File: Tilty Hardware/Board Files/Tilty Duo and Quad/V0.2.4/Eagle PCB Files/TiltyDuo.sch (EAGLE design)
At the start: 49 parts, among them U1 TEENSY_3.0_OUTER-PINS28-DIP_S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, U2 HC-09_BREAKOUT, U3 MPL3115A2LGA8, U4 LM2931, U5 MPU-6050, U6 HMC5883LSMD, U7 SPI_FLASH-X25XXSMD

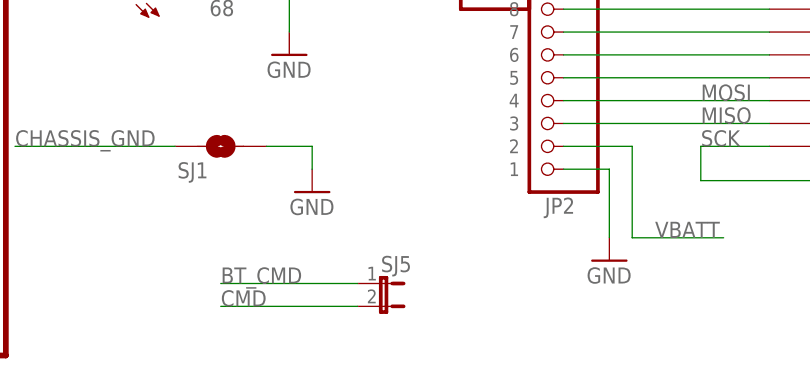
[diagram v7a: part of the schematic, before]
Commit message: Updated bluetooth command jumper to a cuttable trace solder jumper
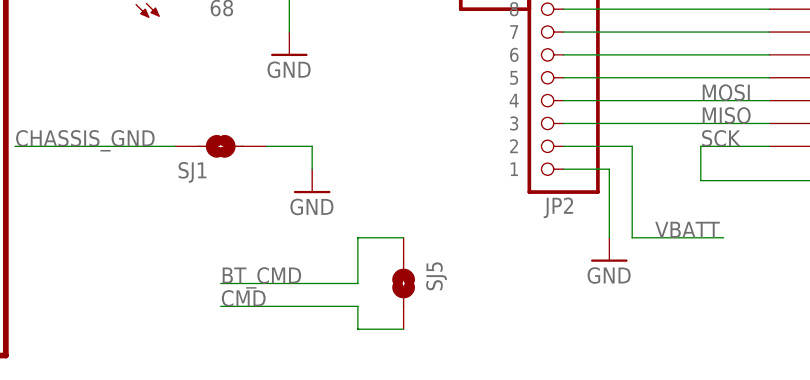
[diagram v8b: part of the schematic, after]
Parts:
- SJ5: value (none) -> SOLDERJUMPERTRACE; device SparkFun-Passives:JUMPER-2SMD-NC -> SparkFun-Passives:SOLDERJUMPERTRACE
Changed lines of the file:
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@@
 <part name="R4" library="resistor" deviceset="R-US_" device="R0603" value="68"/>
 <part name="SJ4" library="SparkFun-Passives" deviceset="SOLDERJUMPER" device="TRACE"/>
-<part name="SJ5" library="SparkFun-Passives" deviceset="JUMPER-2" device="SMD-NC"/>
 <part name="D4" library="SparkFun-DiscreteSemi" deviceset="DIODE" device="SOT23">
 <attribute name="PART#" value="BAT54FSTR-ND"/>
@@
 <part name="SJ6" library="SparkFun-Passives" deviceset="SOLDERJUMPER" device="TRACE"/>
 <part name="D6" library="diode" deviceset="DIODE-" device="DO214AA"/>
+<part name="SJ5" library="SparkFun-Passives" deviceset="SOLDERJUMPER" device="TRACE"/>
 </parts>
 <sheets>
@@
 <attribute name="NAME" x="105.41" y="71.12" size="1.778" layer="95"/>
 </instance>
-<instance part="SJ5" gate="A" x="129.54" y="10.16" rot="R270"/>
 <instance part="D4" gate="G$1" x="218.44" y="60.96" rot="R180">
 <attribute name="PART#" x="218.44" y="60.96" size="1.778" layer="96" rot="R180" display="off"/>
@@
 <attribute name="NAME" x="127" y="121.4374" size="1.778" layer="95" rot="R180"/>
 <attribute name="VALUE" x="124.2314" y="121.92" size="1.778" layer="96" rot="R90"/>
+</instance>
+<instance part="SJ5" gate="1" x="132.08" y="10.16" smashed="yes" rot="R270">
+<attribute name="NAME" x="134.62" y="12.7" size="1.778" layer="95" rot="R270"/>
 </instance>
 </instances>
@@
 <wire x1="127" y1="7.62" x2="111.76" y2="7.62" width="0.1524" layer="91"/>
 <label x="111.76" y="7.62" size="1.778" layer="95"/>
-<pinref part="SJ5" gate="A" pin="2"/>
+<wire x1="127" y1="7.62" x2="127" y2="5.08" width="0.1524" layer="91"/>
+<pinref part="SJ5" gate="1" pin="2"/>
+<wire x1="127" y1="5.08" x2="132.08" y2="5.08" width="0.1524" layer="91"/>
 </segment>
 </net>
@@
 <wire x1="127" y1="10.16" x2="111.76" y2="10.16" width="0.1524" layer="91"/>
 <label x="111.76" y="10.16" size="1.778" layer="95"/>
-<pinref part="SJ5" gate="A" pin="1"/>
-</segment>
-<segment>
+<wire x1="127" y1="10.16" x2="127" y2="15.24" width="0.1524" layer="91"/>
+<pinref part="SJ5" gate="1" pin="1"/>
+<wire x1="127" y1="15.24" x2="132.08" y2="15.24" width="0.1524" layer="91"/>
+</segment>
+<segment>
